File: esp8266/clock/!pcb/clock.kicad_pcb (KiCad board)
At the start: 2 copper layers, 15 parts, among them J1 GPIO, J2 Conn_01x01, J3 Conn_01x01, U1 WeMos_D1_mini, U2 rxb, U3 BME280, U4 oled, U5 led, U6 EMPTY

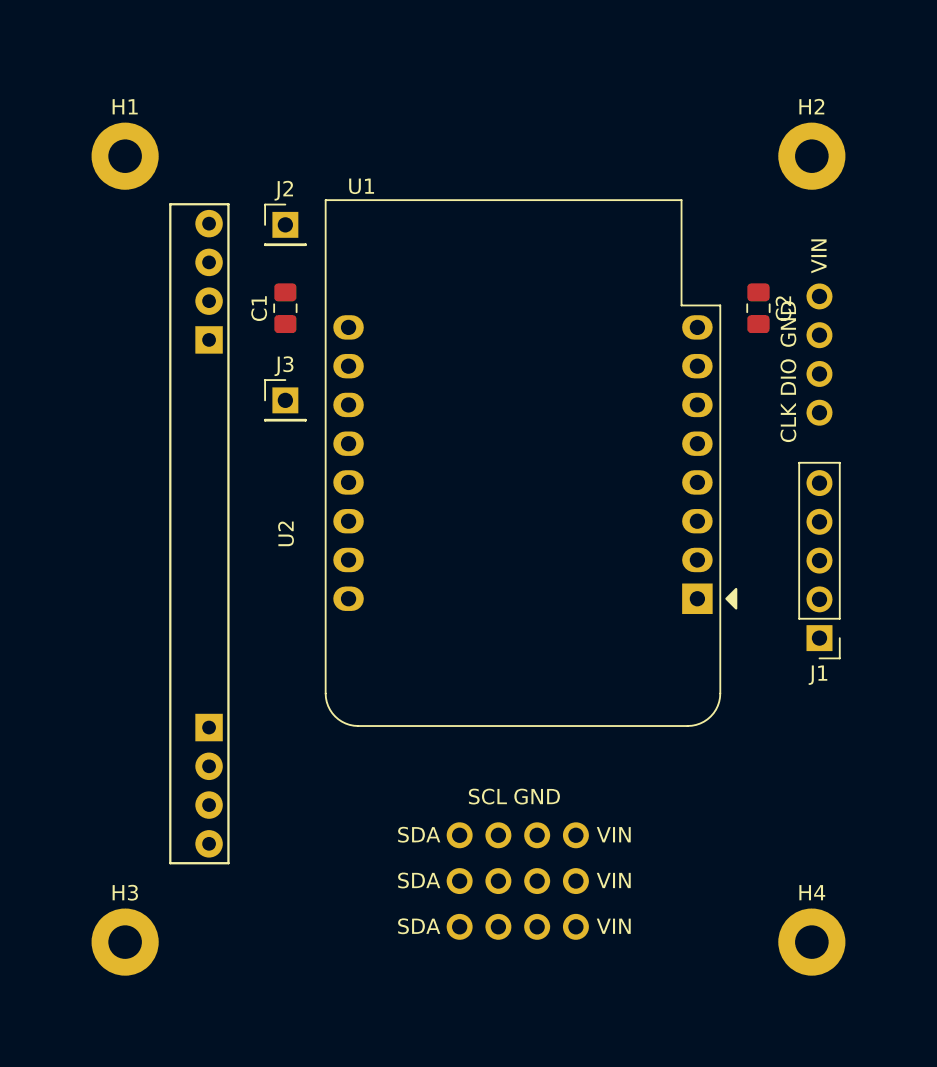
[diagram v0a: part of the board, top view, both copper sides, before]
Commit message: clock: Start routing
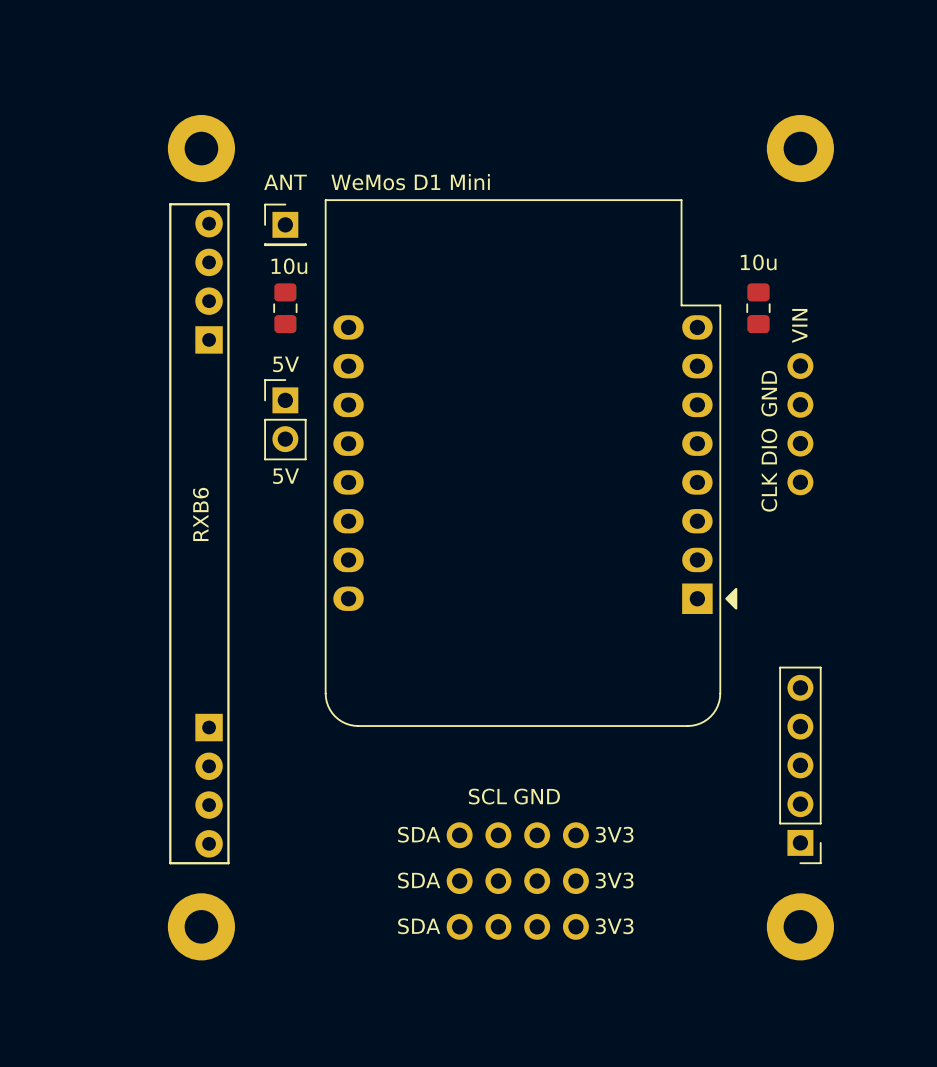
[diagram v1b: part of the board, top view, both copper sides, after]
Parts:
- removed J3: Conn_01x01, Connector_PinHeader_2.54mm:PinHeader_1x01_P2.54mm_Vertical
- added 5V: Conn_01x01, Connector_PinHeader_2.54mm:PinHeader_1x02_P2.54mm_Vertical, F.Cu at (59.0, 80.5)
- RXB6: renamed from U2; value rxb -> RXB6
- U4: value oled -> OLED
- U5: value led -> LED
- U6: value EMPTY -> SPARE
- WeMos D1 Mini: renamed from U1
- moved J1 13.5 mm to (92.8, 109.5)
- moved H3 5.10 mm to (53.5, 115.0)
- moved H1 5.02 mm to (53.5, 64.0)
- moved U5 4.73 mm to (92.8, 82.1)
- moved H4 1.25 mm to (92.8, 115.0)
- moved H2 0.90 mm to (92.8, 64.0)
- renumbered C1 to 10u, C2 to 10u, J2 to ANT
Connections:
- RXB6 pad 3: (no net) -> Net-(U2-Pad3)
- WeMos D1 Mini pad 1: (no net) -> Net-(U1-Pad1)
- WeMos D1 Mini pad 15: (no net) -> Net-(U1-Pad15)
- WeMos D1 Mini pad 16: (no net) -> Net-(U1-Pad16)
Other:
- board text added: "5V"

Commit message: clock: Prepare routing
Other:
- board outline added: 45.2 x 57 mm
- board text added: "A0"
- board text added: "D3"
- board text added: "D4"
- board text added: "D8"
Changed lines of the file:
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@@
   (general
     (thickness 1.6)
-    (drawings 1)
+    (drawings 14)
     (tracks 0)
     (zones 0)
@@
       (effects (font (size 1 1) (thickness 0.15)))
     )
-    (fp_text user SDA (at -6.5 0) (layer F.SilkS)
+    (fp_text user SDA (at -6.5 0) (layer F.Fab)
       (effects (font (size 1 1) (thickness 0.15)))
     )
@@
       (effects (font (size 1 1) (thickness 0.15)))
     )
-    (fp_text user 3V3 (at 6.35 0) (layer F.SilkS)
+    (fp_text user 3V3 (at 6.35 0) (layer F.Fab)
       (effects (font (size 1 1) (thickness 0.15)))
     )
@@
       (effects (font (size 1 1) (thickness 0.15)))
     )
-    (fp_text user 3V3 (at 6.35 0) (layer F.SilkS)
+    (fp_text user 3V3 (at 6.35 0) (layer F.Fab)
       (effects (font (size 1 1) (thickness 0.15)))
     )
@@
       (effects (font (size 1 1) (thickness 0.15)))
     )
-    (fp_text user SDA (at -6.5 0) (layer F.SilkS)
+    (fp_text user SDA (at -6.5 0) (layer F.Fab)
       (effects (font (size 1 1) (thickness 0.15)))
     )
@@
     )
   )
+  (gr_text A0 (at 90.25 109.5) (layer F.SilkS)
+    (effects (font (size 1 1) (thickness 0.15)))
+  )
+  (gr_text D3 (at 90.25 107) (layer F.SilkS)
+    (effects (font (size 1 1) (thickness 0.15)))
+  )
+  (gr_text D3 (at 90.25 104.5) (layer F.SilkS)
+    (effects (font (size 1 1) (thickness 0.15)))
+  )
+  (gr_text D4 (at 90.25 102) (layer F.SilkS)
+    (effects (font (size 1 1) (thickness 0.15)))
+  )
+  (gr_text D8 (at 90.25 99.25) (layer F.SilkS)
+    (effects (font (size 1 1) (thickness 0.15)))
+  )
+  (gr_line (start 50.5 64) (end 50.5 115) (layer Edge.Cuts) (width 0.05))
+  (gr_line (start 95.75 64) (end 95.75 115) (layer Edge.Cuts) (width 0.05))
+  (gr_line (start 53.5 61) (end 92.75 61) (layer Edge.Cuts) (width 0.05))
+  (gr_arc (start 53.5 64) (end 53.5 61) (angle -90) (layer Edge.Cuts) (width 0.05))
+  (gr_arc (start 92.75 64) (end 95.75 64) (angle -90) (layer Edge.Cuts) (width 0.05))
+  (gr_line (start 92.75 118) (end 53.5 118) (layer Edge.Cuts) (width 0.05))
+  (gr_arc (start 92.75 115) (end 92.75 118) (angle -90) (layer Edge.Cuts) (width 0.05))
+  (gr_arc (start 53.5 115) (end 50.5 115) (angle -90) (layer Edge.Cuts) (width 0.05))
   (gr_text 5V (at 59 85.5) (layer F.SilkS)
     (effects (font (size 1 1) (thickness 0.15)))

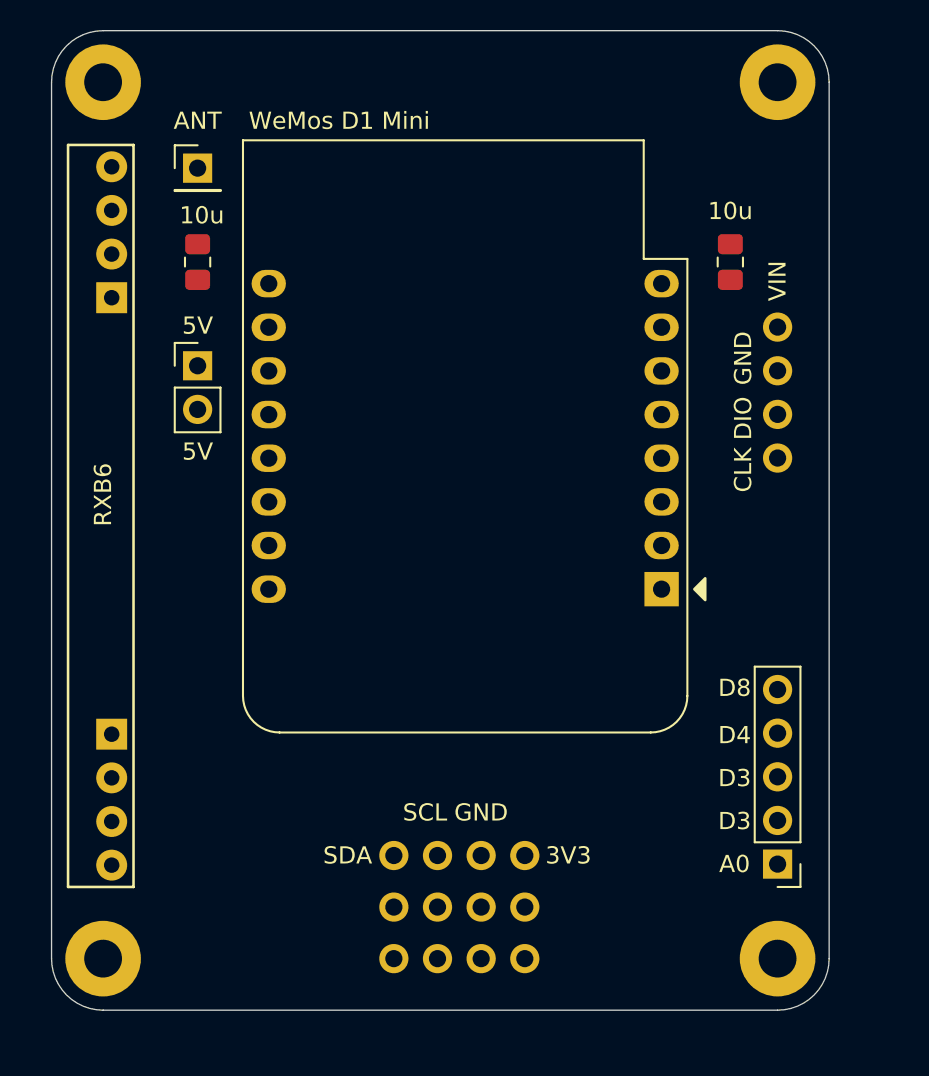
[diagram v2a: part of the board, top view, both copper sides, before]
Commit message: clock: Rough roouting done
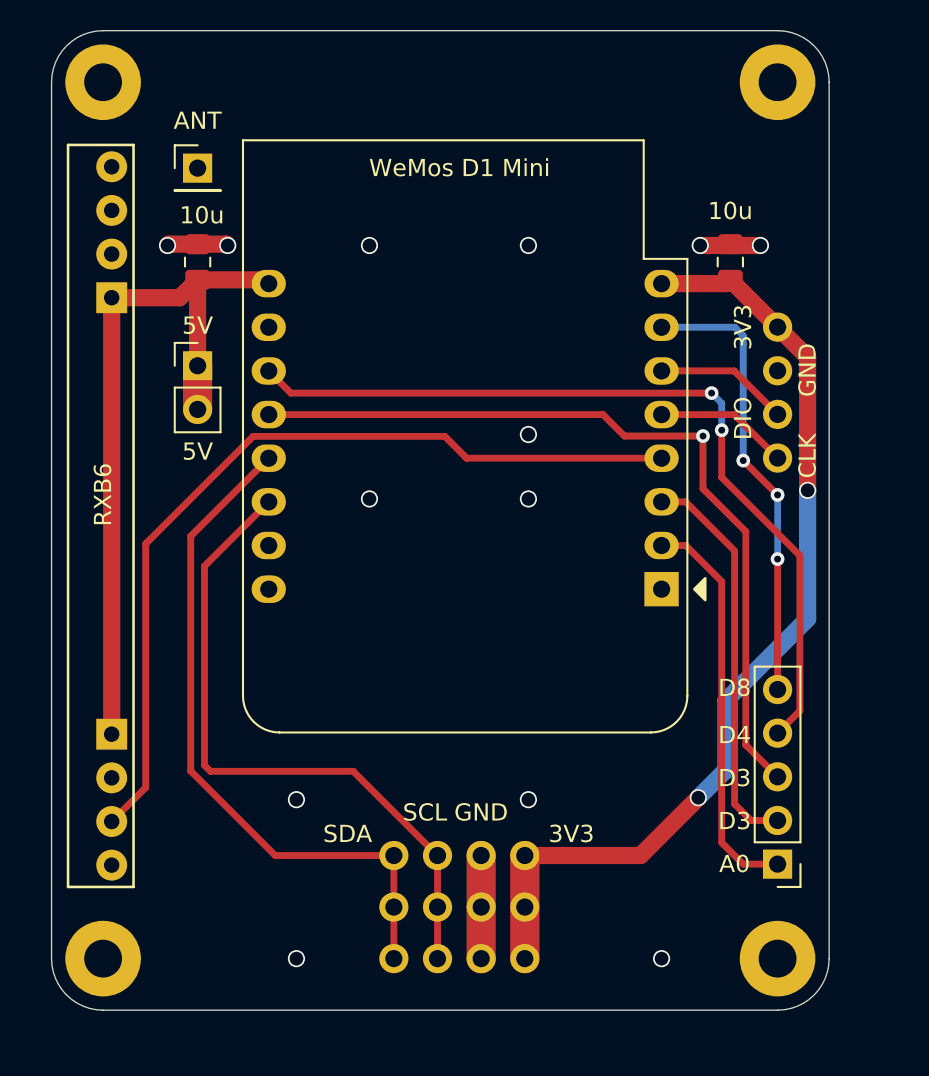
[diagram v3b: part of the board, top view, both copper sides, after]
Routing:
- net +3V3: track 0.00 -> 56.2 mm, vias 0 -> 2
- net DATA: track 0.00 -> 50.1 mm
- net D4: track 0.00 -> 48.8 mm, vias 0 -> 2
- net D3: track 0.00 -> 47.4 mm, vias 0 -> 1
- net +5V: track 0.00 -> 45.1 mm
- net SDA: track 0.00 -> 39.9 mm
- net SCL: track 0.00 -> 38.6 mm
- net D8: track 0.00 -> 26.4 mm, vias 0 -> 3
- net A0: track 0.00 -> 23.3 mm
- net D0: track 0.00 -> 23.1 mm
- net GND: track 0.00 -> 13.1 mm, vias 0 -> 13
- net DIO: track 0.00 -> 7.80 mm
- net CLK: track 0.00 -> 7.80 mm

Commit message: clock: Add dimensions
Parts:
- added G***: LOGO, !myfoots:wifi, F.Cu at (89.8, 69.8)
- added G***: LOGO, !myfoots:microusb, F.Cu at (74.2, 64.0)
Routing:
- net ANT: track 0.00 -> 5.03 mm
- net GND: vias 13 -> 18
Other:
- board text added: "D0"
- board text added: "JLCJLCJLCJLC"
- board text added: "https://github.com/tantecky/embedded"
- board text added: "v1.0"

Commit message: clock: Almost ready
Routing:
- net GND: track 13.1 -> 15.6 mm
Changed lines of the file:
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@@
     (thickness 1.6)
     (drawings 23)
-    (tracks 111)
+    (tracks 112)
     (zones 0)
     (modules 17)
@@
       (outputformat 1)
       (mirror false)
-      (drillshape 1)
+      (drillshape 0)
       (scaleselection 1)
-      (outputdirectory ""))
+      (outputdirectory "gerbs/"))
   )
   (net 0 "")
@@
       (effects (font (size 0.5 0.5) (thickness 0.08)))
     )
-    (pad 1 smd roundrect (at -1.0375 0 90) (size 1.175 1.45) (layers F.Cu F.Paste F.Mask) (roundrect_rratio 0.212766)
+    (pad 1 smd roundrect (at -1.0375 0 90) (size 1.175 1.45) (layers F.Cu F.Paste F.Mask) (roundrect_rratio 0.2127659574468085)
       (net 1 +5V))
-    (pad 2 smd roundrect (at 1.0375 0 90) (size 1.175 1.45) (layers F.Cu F.Paste F.Mask) (roundrect_rratio 0.212766)
+    (pad 2 smd roundrect (at 1.0375 0 90) (size 1.175 1.45) (layers F.Cu F.Paste F.Mask) (roundrect_rratio 0.2127659574468085)
       (net 2 GND))
     (model ${KISYS3DMOD}/Capacitor_SMD.3dshapes/C_0805_2012Metric.wrl
@@
       (effects (font (size 0.5 0.5) (thickness 0.08)))
     )
-    (pad 2 smd roundrect (at 1.0375 0 270) (size 1.175 1.45) (layers F.Cu F.Paste F.Mask) (roundrect_rratio 0.212766)
+    (pad 2 smd roundrect (at 1.0375 0 270) (size 1.175 1.45) (layers F.Cu F.Paste F.Mask) (roundrect_rratio 0.2127659574468085)
       (net 3 +3V3))
-    (pad 1 smd roundrect (at -1.0375 0 270) (size 1.175 1.45) (layers F.Cu F.Paste F.Mask) (roundrect_rratio 0.212766)
+    (pad 1 smd roundrect (at -1.0375 0 270) (size 1.175 1.45) (layers F.Cu F.Paste F.Mask) (roundrect_rratio 0.2127659574468085)
       (net 2 GND))
     (model ${KISYS3DMOD}/Capacitor_SMD.3dshapes/C_0805_2012Metric.wrl
@@
   (via (at 56.75 85.5) (size 1) (drill 0.8) (layers F.Cu B.Cu) (net 2))
   (via (at 57.25 109.5) (size 1) (drill 0.8) (layers F.Cu B.Cu) (net 2))
+  (segment (start 54 71.46) (end 54 74) (width 1) (layer F.Cu) (net 2))
   (segment (start 84.772808 109) (end 78.04 109) (width 1) (layer F.Cu) (net 3))
   (segment (start 94.500001 80.000001) (end 94.500001 87.749999) (width 1) (layer F.Cu) (net 3))
